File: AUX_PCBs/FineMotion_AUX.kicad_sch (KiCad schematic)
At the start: 11 parts, among them J2 Conn_01x04_Female, U1 ME6211C, U9 MPU-9250

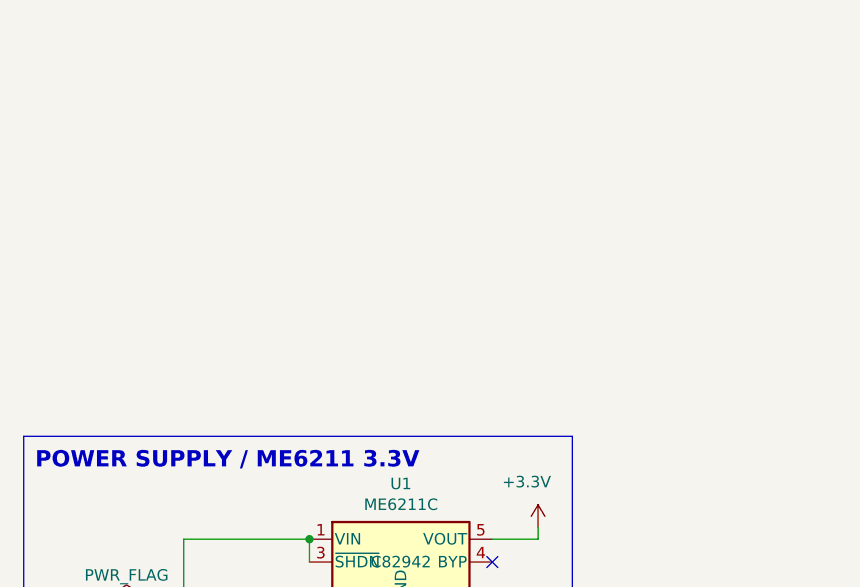
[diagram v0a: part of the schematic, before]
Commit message: Placement of pads to assemble the BNO085 module
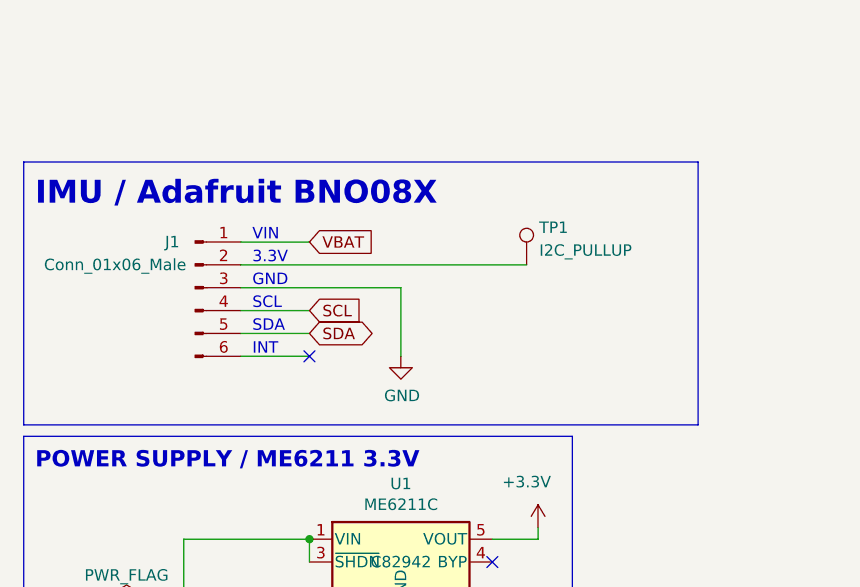
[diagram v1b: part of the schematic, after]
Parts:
- added J1: Conn_01x06_Male, Connector_PinHeader_2.54mm:PinHeader_1x06_P2.54mm_Vertical, symbol Connector:Conn_01x06_Male
- added TP1: I2C_PULLUP, TestPoint:TestPoint_Pad_D1.5mm, symbol Connector:TestPoint
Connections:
- net GND: now also J1.3 (Pin_3)
- net SCL: now also J1.4 (Pin_4)
- net SDA: now also J1.5 (Pin_5)
- net VBAT: now also J1.1 (Pin_1)
- new net: J1.2 (Pin_2), TP1.1
- no-connect marks 5 -> 6
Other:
- note added: "3.3V"
- note added: "GND"
- note added: "IMU / Adafruit BNO08X"
- note added: "INT"
- note added: "SCL"
- note added: "SDA"
- note added: "VIN"
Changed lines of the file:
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@@
   (no_connect (at 256.54 55.88))
   (no_connect (at 256.54 48.26))
+  (no_connect (at 54.61 123.19))
   (wire (pts (xy 210.82 21.59) (xy 210.82 43.18))
     (stroke (width 0) (type default) (color 0 0 0 0))
   )
+  (polyline (pts (xy 22.86 101.6) (xy 22.86 130.81))
+    (stroke (width 0) (type default) (color 0 0 0 0))
+  )
   (wire (pts (xy 256.54 71.12) (xy 238.76 71.12))
     (stroke (width 0) (type default) (color 0 0 0 0))
   )
+  (wire (pts (xy 46.99 113.03) (xy 78.74 113.03))
+    (stroke (width 0) (type default) (color 0 0 0 0))
+  )
   (polyline (pts (xy 50.8 195.58) (xy 50.8 175.26))
     (stroke (width 0) (type default) (color 0 0 0 0))
   )
+  (polyline (pts (xy 97.79 101.6) (xy 97.79 130.81))
+    (stroke (width 0) (type default) (color 0 0 0 0))
+  )
   (wire (pts (xy 43.18 162.56) (xy 35.56 162.56))
     (stroke (width 0) (type default) (color 0 0 0 0))
@@
     (stroke (width 0) (type default) (color 0 0 0 0))
   )
+  (wire (pts (xy 46.99 123.19) (xy 54.61 123.19))
+    (stroke (width 0) (type default) (color 0 0 0 0))
+  )
   (wire (pts (xy 189.23 54.61) (xy 193.04 54.61))
     (stroke (width 0) (type default) (color 0 0 0 0))
@@
     (stroke (width 0) (type default) (color 0 0 0 0))
   )
+  (polyline (pts (xy 97.79 130.81) (xy 22.86 130.81))
+    (stroke (width 0) (type default) (color 0 0 0 0))
+  )
   (wire (pts (xy 210.82 21.59) (xy 217.17 21.59))
     (stroke (width 0) (type default) (color 0 0 0 0))
@@
     (stroke (width 0) (type default) (color 0 0 0 0))
   )
+  (wire (pts (xy 46.99 115.57) (xy 64.77 115.57))
+    (stroke (width 0) (type default) (color 0 0 0 0))
+  )
   (wire (pts (xy 40.64 158.75) (xy 64.77 158.75))
     (stroke (width 0) (type default) (color 0 0 0 0))
@@
     (stroke (width 0) (type default) (color 0 0 0 0))
   )
+  (wire (pts (xy 64.77 115.57) (xy 64.77 123.19))
+    (stroke (width 0) (type default) (color 0 0 0 0))
+  )
   (wire (pts (xy 220.98 53.34) (xy 210.82 53.34))
     (stroke (width 0) (type default) (color 0 0 0 0))
@@
     (stroke (width 0) (type default) (color 0 0 0 0))
   )
+  (wire (pts (xy 46.99 110.49) (xy 54.61 110.49))
+    (stroke (width 0) (type default) (color 0 0 0 0))
+  )
   (wire (pts (xy 200.66 21.59) (xy 210.82 21.59))
     (stroke (width 0) (type default) (color 0 0 0 0))
@@
     (stroke (width 0) (type default) (color 0 0 0 0))
   )
+  (polyline (pts (xy 22.86 101.6) (xy 97.79 101.6))
+    (stroke (width 0) (type default) (color 0 0 0 0))
+  )
   (wire (pts (xy 27.94 187.96) (xy 36.83 187.96))
     (stroke (width 0) (type default) (color 0 0 0 0))
@@
     (stroke (width 0) (type default) (color 0 0 0 0))
   )
+  (wire (pts (xy 46.99 120.65) (xy 54.61 120.65))
+    (stroke (width 0) (type default) (color 0 0 0 0))
+  )
   (wire (pts (xy 31.75 180.34) (xy 36.83 180.34))
     (stroke (width 0) (type default) (color 0 0 0 0))
   )
   (wire (pts (xy 217.17 48.26) (xy 217.17 21.59))
+    (stroke (width 0) (type default) (color 0 0 0 0))
+  )
+  (wire (pts (xy 46.99 118.11) (xy 54.61 118.11))
     (stroke (width 0) (type default) (color 0 0 0 0))
   )
@@
     (effects (font (size 1.27 1.27) (thickness 0.254) bold) (justify left bottom))
   )
+  (text "SCL" (at 48.26 118.11 0)
+    (effects (font (size 1.27 1.27)) (justify left bottom))
+  )
   (text "IMU / MPU-6500" (at 184.15 20.32 0)
     (effects (font (size 2.54 2.54) (thickness 0.508) bold) (justify left bottom))
   )
+  (text "SDA" (at 48.26 120.65 0)
+    (effects (font (size 1.27 1.27)) (justify left bottom))
+  )
+  (text "IMU / Adafruit BNO08X" (at 24.13 106.68 0)
+    (effects (font (size 2.54 2.54) (thickness 0.508) bold) (justify left bottom))
+  )
   (text "POWER SUPPLY / ME6211 3.3V" (at 24.13 135.89 0)
     (effects (font (size 1.8034 1.8034) (thickness 0.3607) bold) (justify left bottom))
+  )
+  (text "GND" (at 48.26 115.57 0)
+    (effects (font (size 1.27 1.27)) (justify left bottom))
+  )
+  (text "VIN" (at 48.26 110.49 0)
+    (effects (font (size 1.27 1.27)) (justify left bottom))
+  )
+  (text "INT" (at 48.26 123.19 0)
+    (effects (font (size 1.27 1.27)) (justify left bottom))
+  )
+  (text "3.3V" (at 48.26 113.03 0)
+    (effects (font (size 1.27 1.27)) (justify left bottom))
   )
   (global_label "VBAT" (shape input) (at 31.75 180.34 180) (fields_autoplaced)
@@
     )
   )
+  (global_label "SCL" (shape input) (at 54.61 118.11 0) (fields_autoplaced)
+    (effects (font (size 1.27 1.27)) (justify left))
+    (property "Intersheet References" "${INTERSHEET_REFS}" (id 0) (at 236.22 254 0)
+      (effects (font (size 1.27 1.27)) hide)
+    )
+  )
   (global_label "VBAT" (shape output) (at 30.48 151.13 180) (fields_autoplaced)
     (effects (font (size 1.27 1.27)) (justify right))
@@
     (property "Intersheet References" "${INTERSHEET_REFS}" (id 0) (at 0 0 0)
       (effects (font (size 1.27 1.27)) hide)
+    )
+  )
+  (global_label "VBAT" (shape input) (at 54.61 110.49 0) (fields_autoplaced)
+    (effects (font (size 1.27 1.27)) (justify left))
+    (property "Intersheet References" "${INTERSHEET_REFS}" (id 0) (at 61.349 110.4106 0)
+      (effects (font (size 1.27 1.27)) (justify left) hide)
+    )
+  )
+  (global_label "SDA" (shape bidirectional) (at 54.61 120.65 0) (fields_autoplaced)
+    (effects (font (size 1.27 1.27)) (justify left))
+    (property "Intersheet References" "${INTERSHEET_REFS}" (id 0) (at 60.5023 120.5706 0)
+      (effects (font (size 1.27 1.27)) (justify left) hide)
     )
   )
@@
     (pin "9")
   )
+  (symbol (lib_id "power:GND") (at 64.77 123.19 0) (unit 1)
+    (in_bom yes) (on_board yes)
+    (property "Reference" "#PWR0102" (id 0) (at 64.77 129.54 0)
+      (effects (font (size 1.27 1.27)) hide)
+    )
+    (property "Value" "GND" (id 1) (at 64.897 127.5842 0))
+    (property "Footprint" "" (id 2) (at 64.77 123.19 0)
+      (effects (font (size 1.27 1.27)) hide)
+    )
+    (property "Datasheet" "" (id 3) (at 64.77 123.19 0)
+      (effects (font (size 1.27 1.27)) hide)
+    )
+    (pin "1")
+  )
+  (symbol (lib_id "Connector:Conn_01x06_Male") (at 41.91 115.57 0) (unit 1)
+    (in_bom yes) (on_board yes)
+    (property "Reference" "J1" (id 0) (at 39.37 110.49 0))
+    (property "Value" "Conn_01x06_Male" (id 1) (at 33.02 113.03 0))
+    (property "Footprint" "Connector_PinHeader_2.54mm:PinHeader_1x06_P2.54mm_Vertical" (id 2) (at 41.91 115.57 0)
+      (effects (font (size 1.27 1.27)) hide)
+    )
+    (property "Datasheet" "~" (id 3) (at 41.91 115.57 0)
+      (effects (font (size 1.27 1.27)) hide)
+    )
+    (pin "1")
+    (pin "2")
+    (pin "3")
+    (pin "4")
+    (pin "5")
+    (pin "6")
+  )
+  (symbol (lib_id "Connector:TestPoint") (at 78.74 113.03 0) (unit 1)
+    (in_bom yes) (on_board yes) (fields_autoplaced)
+    (property "Reference" "TP1" (id 0) (at 80.137 108.8933 0)
+      (effects (font (size 1.27 1.27)) (justify left))
+    )
+    (property "Value" "I2C_PULLUP" (id 1) (at 80.137 111.4302 0)
+      (effects (font (size 1.27 1.27)) (justify left))
+    )
+    (property "Footprint" "TestPoint:TestPoint_Pad_D1.5mm" (id 2) (at 83.82 113.03 0)
+      (effects (font (size 1.27 1.27)) hide)
+    )
+    (property "Datasheet" "~" (id 3) (at 83.82 113.03 0)
+      (effects (font (size 1.27 1.27)) hide)
+    )
+    (pin "1")
+  )
   (symbol (lib_id "Device:C") (at 275.59 48.26 180) (unit 1)
     (in_bom yes) (on_board yes)
@@
       (reference "#PWR0101") (unit 1) (value "GND") (footprint "")
     )
+    (path "/b30041c3-afcd-4d42-a374-8e4908b11d9a"
+      (reference "#PWR0102") (unit 1) (value "GND") (footprint "")
+    )
     (path "/00000000-0000-0000-0000-000061f70f5d"
       (reference "#PWR0109") (unit 1) (value "+3.3V") (footprint "")
@@
       (reference "C21") (unit 1) (value "0.1uF") (footprint "Capacitor_SMD:C_0402_1005Metric")
     )
+    (path "/c66998fa-5623-4e67-a6aa-7d08562f336f"
+      (reference "J1") (unit 1) (value "Conn_01x06_Male") (footprint "Connector_PinHeader_2.54mm:PinHeader_1x06_P2.54mm_Vertical")
+    )
     (path "/00000000-0000-0000-0000-000062288446"
       (reference "J2") (unit 1) (value "Conn_01x04_Female") (footprint "Connector_JST:JST_PH_S4B-PH-K_1x04_P2.00mm_Horizontal")
@@
       (reference "R12") (unit 1) (value "2.2K") (footprint "Resistor_SMD:R_0402_1005Metric")
     )
+    (path "/d442b826-5f9c-4541-a593-0728a766a461"
+      (reference "TP1") (unit 1) (value "I2C_PULLUP") (footprint "TestPoint:TestPoint_Pad_D1.5mm")
+    )
     (path "/00000000-0000-0000-0000-000062335044"
